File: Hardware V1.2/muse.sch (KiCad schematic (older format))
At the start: 55 parts, among them P1 3.5mm_line, P2 3.5mm_line, P3 RCA, P4 RCA, P5 ATX_PWR_OK, P6 ATX_PWR, P7 ATX_GND, P8 ATX_PS_ON, P9 LED_Signal, Q1 FQP30N06L, Q2 FQP30N06L, Q3 FQP30N06L, Q4 FQP30N06L, Q5 FQP30N06L, Q6 FQP30N06L, U1 MSGEQ7, U2 MSGEQ7, U3 74LS595, U4 Spark_Core

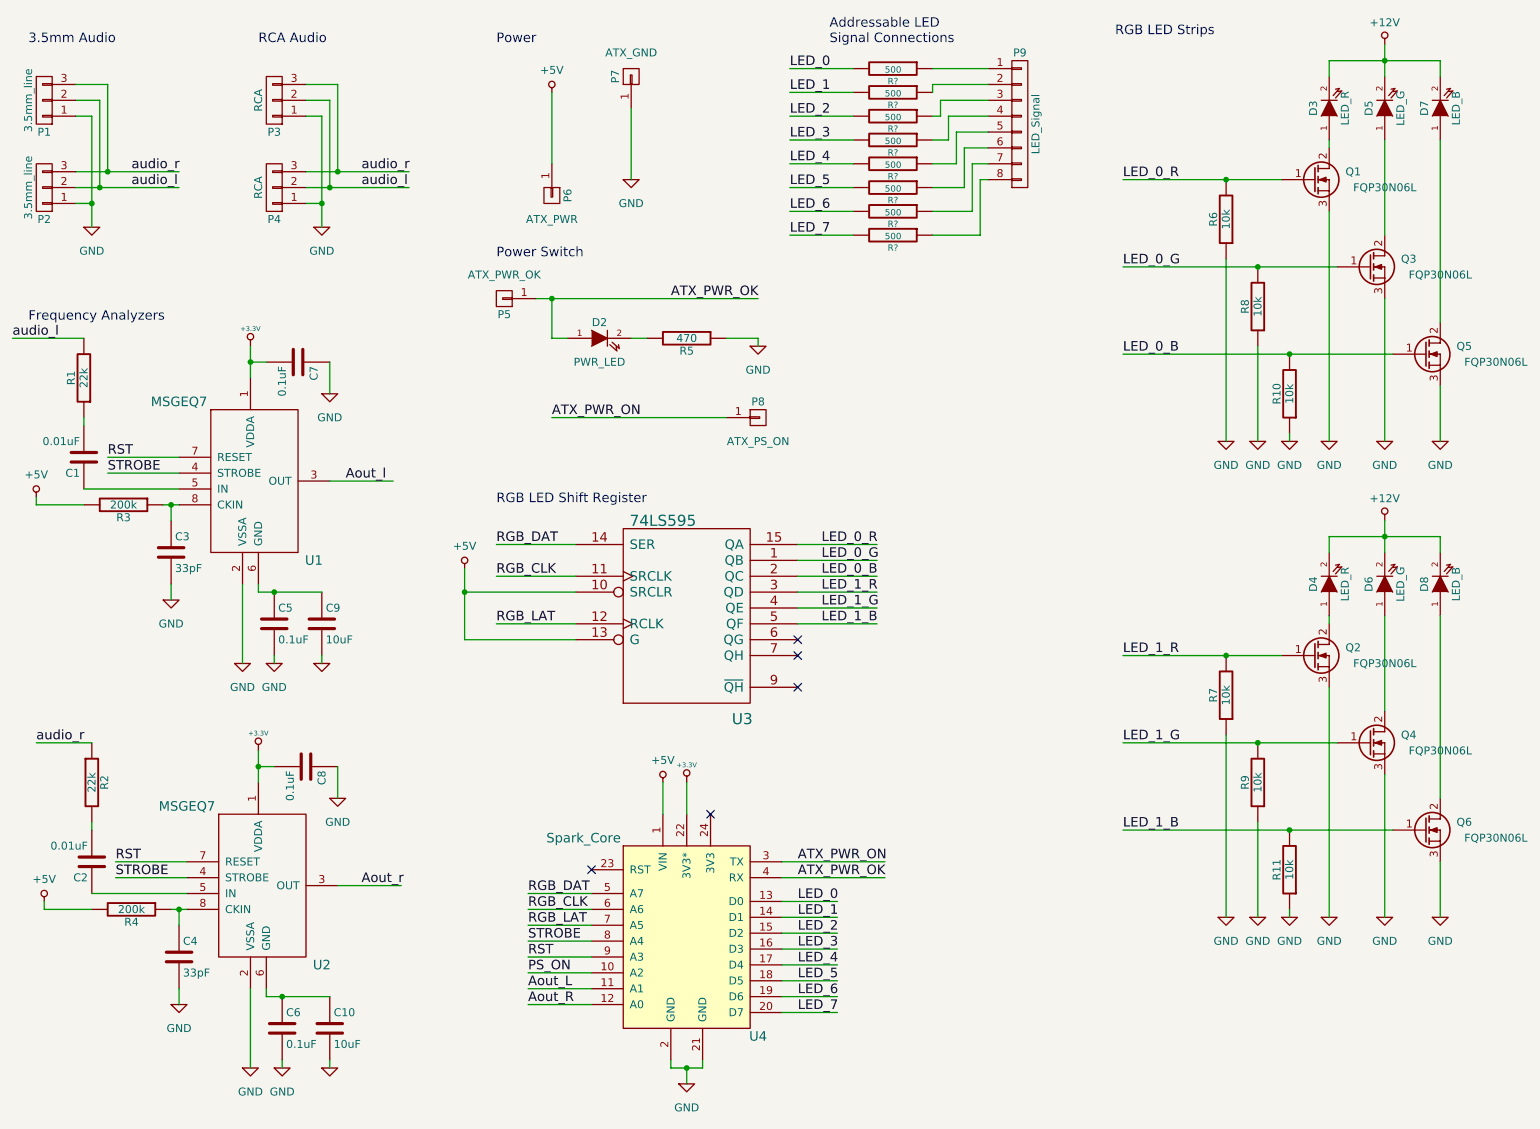
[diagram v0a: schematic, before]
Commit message: Updated power paths and RF keepouts
Currently editing transistor GND path sizes
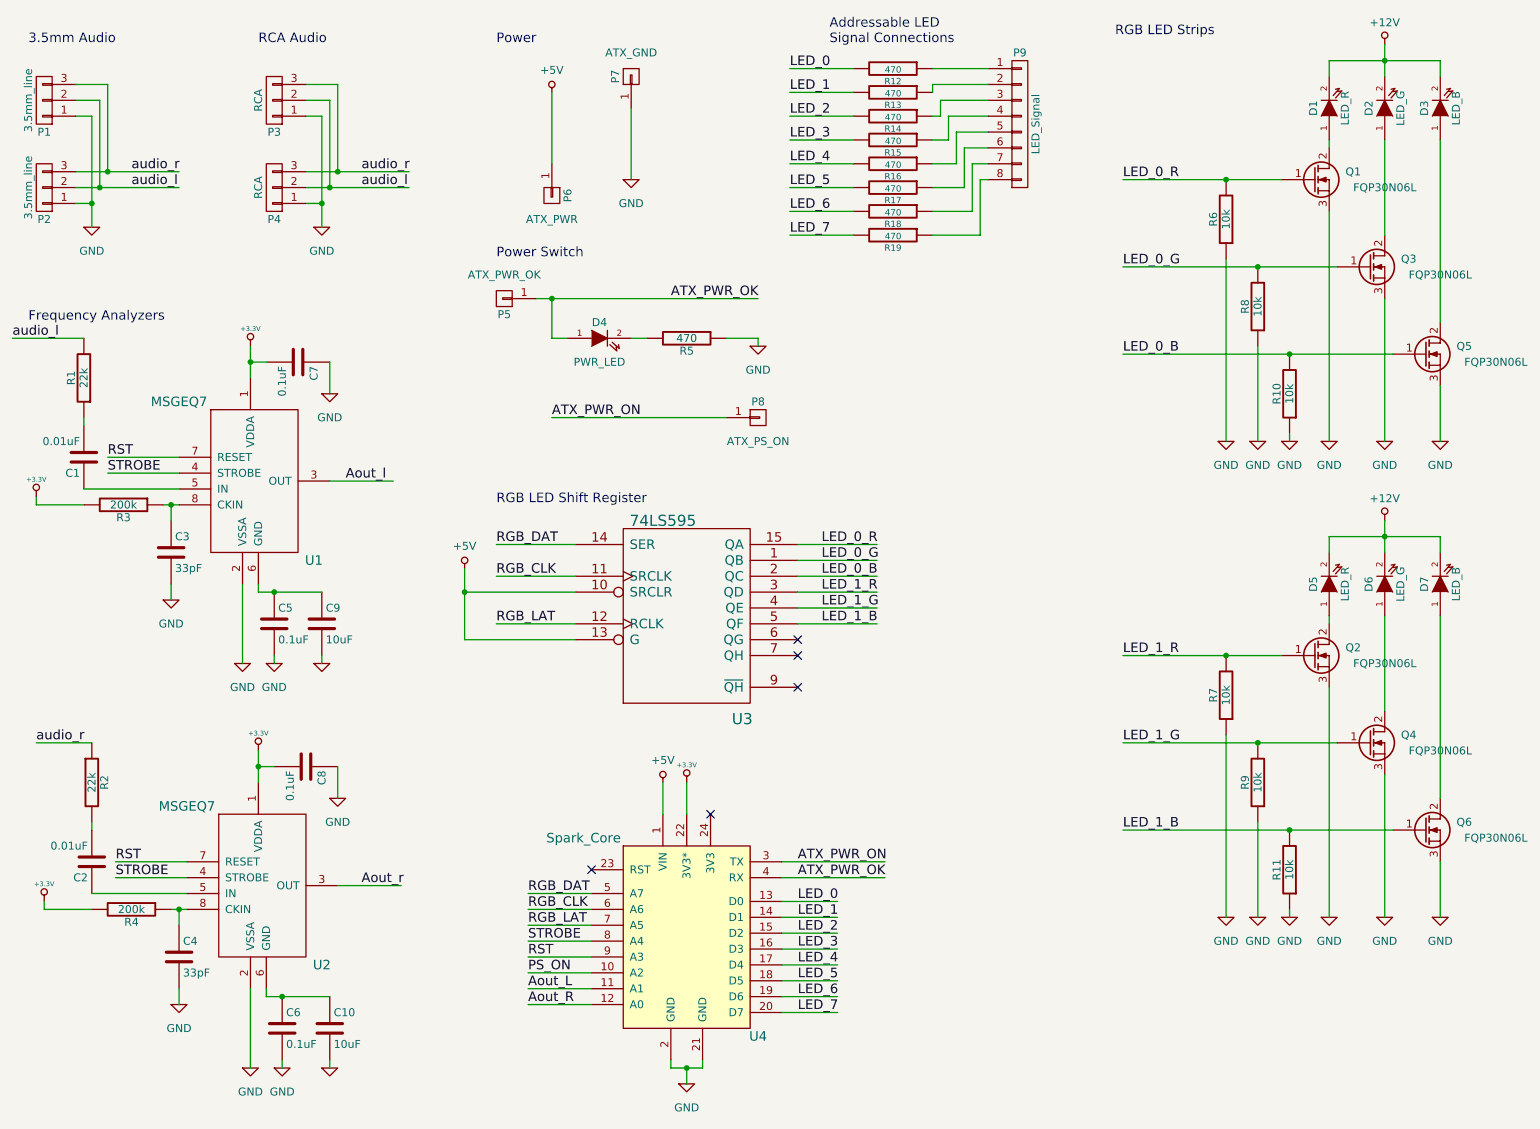
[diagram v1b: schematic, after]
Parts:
- R12, R13, R14, R15, R16, R17, R18, R19: renamed from R?; value 500 -> 470; footprint (none) -> Resistors_ThroughHole:Resistor_Horizontal_RM10mm
- renumbered D3 to D1, D5 to D2, D7 to D3, D2 to D4, D4 to D5, D8 to D7
